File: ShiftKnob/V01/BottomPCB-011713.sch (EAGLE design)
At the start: 39 parts, among them IC2 7805DT, Q1 16MHz, Q2 MOSFET-NCHANNELSMD, Q3 MOSFET-NCHANNELSMD, Q4 MOSFET-NCHANNELSMD, Q5 MOSFET-NCHANNELSMD, Q6 MOSFET-NCHANNELSMD, U1 ATMEGA328

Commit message: preliminarily finalized. added silk screen labels. may still add mounting holes
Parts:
- JP2: device SparkFun:ARDUINO_SERIAL_PROGRAMPTH -> SparkFun-Connectors:M06SIP
- U$11: value LOGO-SFENEW -> LOGO-SFESK; device SparkFun:LOGO-SFENEW -> SparkFun:LOGO-SFESK
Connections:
- net DTR: now also JP2.1; no longer JP2.DTR
- net GND: now also JP2.5, JP2.6; no longer JP2.CTS, JP2.GND
- net RXI: now also JP2.3; no longer JP2.TXO
- net TXO: now also JP2.2; no longer JP2.RXI
- net VUSB: now also JP2.4; no longer JP2.VCC
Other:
- moved on the sheet: JP2
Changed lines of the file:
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@@
 <part name="C1" library="SparkFun" deviceset="CAP" device="0402-CAP" value="0.1uF"/>
 <part name="GND7" library="SparkFun" deviceset="GND" device=""/>
-<part name="U$11" library="SparkFun" deviceset="LOGO-SFE" device="NEW"/>
+<part name="U$11" library="SparkFun" deviceset="LOGO-SFE" device="SK" value="LOGO-SFESK"/>
 <part name="P+11" library="SparkFun" deviceset="3.3V" device="" value="VCC"/>
 <part name="P+15" library="SparkFun" deviceset="3.3V" device="" value="VCC"/>
@@
 <part name="P+1" library="SparkFun" deviceset="3.3V" device="" value="VCC"/>
 <part name="GND5" library="SparkFun" deviceset="GND" device=""/>
-<part name="JP2" library="SparkFun" deviceset="ARDUINO_SERIAL_PROGRAM" device="PTH" value="FTDI Basic"/>
+<part name="JP2" library="SparkFun-Connectors" deviceset="M06" device="SIP" value="FTDI Basic"/>
 <part name="C2" library="SparkFun" deviceset="CAP" device="0402-CAP" value="0.1uF"/>
 <part name="U$3" library="SparkFun" deviceset="OSHW-LOGO" device="S"/>
@@
 <wire x1="25.4" y1="195.58" x2="33.02" y2="195.58" width="0.1524" layer="91"/>
 <label x="27.94" y="195.58" size="1.778" layer="95"/>
-<pinref part="JP2" gate="G$1" pin="CTS"/>
+<pinref part="JP2" gate="G$1" pin="5"/>
 </segment>
 <segment>
 <wire x1="25.4" y1="198.12" x2="33.02" y2="198.12" width="0.1524" layer="91"/>
 <label x="27.94" y="198.12" size="1.778" layer="95"/>
-<pinref part="JP2" gate="G$1" pin="GND"/>
+<pinref part="JP2" gate="G$1" pin="6"/>
 </segment>
 <segment>
@@
 <wire x1="25.4" y1="187.96" x2="33.02" y2="187.96" width="0.1524" layer="91"/>
 <label x="27.94" y="187.96" size="1.778" layer="95"/>
-<pinref part="JP2" gate="G$1" pin="RXI"/>
+<pinref part="JP2" gate="G$1" pin="2"/>
 </segment>
 </net>
@@
 <wire x1="25.4" y1="185.42" x2="33.02" y2="185.42" width="0.1524" layer="91"/>
 <label x="27.94" y="185.42" size="1.778" layer="95"/>
-<pinref part="JP2" gate="G$1" pin="DTR"/>
+<pinref part="JP2" gate="G$1" pin="1"/>
 </segment>
 <segment>
@@
 <wire x1="25.4" y1="190.5" x2="33.02" y2="190.5" width="0.1524" layer="91"/>
 <label x="27.94" y="190.5" size="1.778" layer="95"/>
-<pinref part="JP2" gate="G$1" pin="TXO"/>
+<pinref part="JP2" gate="G$1" pin="3"/>
 </segment>
 <segment>
@@
 <wire x1="25.4" y1="193.04" x2="33.02" y2="193.04" width="0.1524" layer="91"/>
 <label x="27.94" y="193.04" size="1.778" layer="95"/>
-<pinref part="JP2" gate="G$1" pin="VCC"/>
-</segment>
-<segment>
+<pinref part="JP2" gate="G$1" pin="4"/>
+</segment>
+<segment>

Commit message: change diodes to match. add silk screen for polarity marking.
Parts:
- D1: value MBRA140 -> MBR0520LT; device SparkFun-DiscreteSemi:MBRA140 -> diode:MBR0520LT
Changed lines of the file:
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@@
 <part name="VCC2" library="SparkFun" deviceset="3.3V" device="" value="VCC"/>
 <part name="JP4" library="SparkFun-Connectors" deviceset="M02" device="-JST-2MM-SMT" value="PWM Motor Connection"/>
-<part name="D1" library="SparkFun-DiscreteSemi" deviceset="MBRA140" device=""/>
+<part name="D1" library="diode" deviceset="MBR0520LT" device=""/>
 <part name="GND8" library="SparkFun" deviceset="GND" device=""/>
 <part name="LED1" library="SparkFun" deviceset="LED-TRICOLOR" device=""/>

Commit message: attach button to arduino pin 2 rather than 12 to use internal interrupt. adjust board accordingly. remove resistor and use internal resistor of atemga328.
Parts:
- removed R12: 10k, SparkFun-Passives:RESISTOR0402-RES
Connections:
- net D12: no longer R12.1, S1.3, S1.4
- net D2: now also S1.3, S1.4
- net VCC: no longer R12.2
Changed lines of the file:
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@@
 <part name="GND13" library="SparkFun" deviceset="GND" device=""/>
 <part name="GND14" library="SparkFun" deviceset="GND" device=""/>
-<part name="P+2" library="SparkFun" deviceset="3.3V" device="" value="VCC"/>
-<part name="R12" library="SparkFun-Passives" deviceset="RESISTOR" device="0402-RES" value="10k"/>
 <part name="D2" library="diode" deviceset="MBR0520LT" device=""/>
 <part name="VUSB" library="SparkFun-Aesthetics" deviceset="VCC" device="" value="VUSB"/>
@@
 <instance part="GND13" gate="1" x="160.02" y="58.42"/>
 <instance part="GND14" gate="1" x="175.26" y="43.18"/>
-<instance part="P+2" gate="G$1" x="119.38" y="71.12" smashed="yes">
-<attribute name="VALUE" x="120.904" y="74.676" size="1.778" layer="96"/>
-</instance>
-<instance part="R12" gate="G$1" x="119.38" y="63.5" smashed="yes" rot="R90">
-<attribute name="NAME" x="125.73" y="67.0814" size="1.778" layer="95" rot="R180"/>
-<attribute name="VALUE" x="125.73" y="61.722" size="1.778" layer="96" rot="R180"/>
-</instance>
 <instance part="D2" gate="G$1" x="149.86" y="187.96" rot="MR0"/>
 <instance part="VUSB" gate="1" x="157.48" y="193.04" rot="MR0"/>
@@
 </segment>
 <segment>
-<pinref part="R12" gate="G$1" pin="2"/>
-<pinref part="P+2" gate="G$1" pin="3.3V"/>
-<wire x1="119.38" y1="71.12" x2="119.38" y2="68.58" width="0.1524" layer="91"/>
-</segment>
-<segment>
 <pinref part="D2" gate="G$1" pin="C"/>
 <wire x1="147.32" y1="187.96" x2="139.7" y2="187.96" width="0.1524" layer="91"/>
@@
 <label x="101.6" y="76.2" size="1.778" layer="95"/>
 <pinref part="U1" gate="G$1" pin="PB4(MISO)"/>
-<pinref part="S1" gate="S" pin="3"/>
-<wire x1="99.06" y1="76.2" x2="116.84" y2="76.2" width="0.1524" layer="91"/>
-<wire x1="116.84" y1="76.2" x2="116.84" y2="58.42" width="0.1524" layer="91"/>
-<wire x1="116.84" y1="58.42" x2="116.84" y2="53.34" width="0.1524" layer="91"/>
-<pinref part="S1" gate="S" pin="4"/>
-<wire x1="116.84" y1="58.42" x2="119.38" y2="58.42" width="0.1524" layer="91"/>
-<wire x1="119.38" y1="58.42" x2="119.38" y2="53.34" width="0.1524" layer="91"/>
-<junction x="116.84" y="58.42"/>
-<pinref part="R12" gate="G$1" pin="1"/>
-<junction x="119.38" y="58.42"/>
+<wire x1="99.06" y1="76.2" x2="111.76" y2="76.2" width="0.1524" layer="91"/>
 </segment>
 </net>
@@
 <net name="D2" class="0">
 <segment>
-<wire x1="99.06" y1="104.14" x2="109.22" y2="104.14" width="0.1524" layer="91"/>
+<wire x1="99.06" y1="104.14" x2="116.84" y2="104.14" width="0.1524" layer="91"/>
 <label x="101.6" y="104.14" size="1.778" layer="95"/>
 <pinref part="U1" gate="G$1" pin="PD2(INT0)"/>
-</segment>
-</net>
+<pinref part="S1" gate="S" pin="3"/>
+<pinref part="S1" gate="S" pin="4"/>
+<wire x1="119.38" y1="58.42" x2="119.38" y2="53.34" width="0.1524" layer="91"/>
+<wire x1="116.84" y1="58.42" x2="119.38" y2="58.42" width="0.1524" layer="91"/>
+<wire x1="116.84" y1="58.42" x2="116.84" y2="53.34" width="0.1524" layer="91"/>
+<wire x1="116.84" y1="58.42" x2="116.84" y2="104.14" width="0.1524" layer="91"/>
+</segment>
+</net>

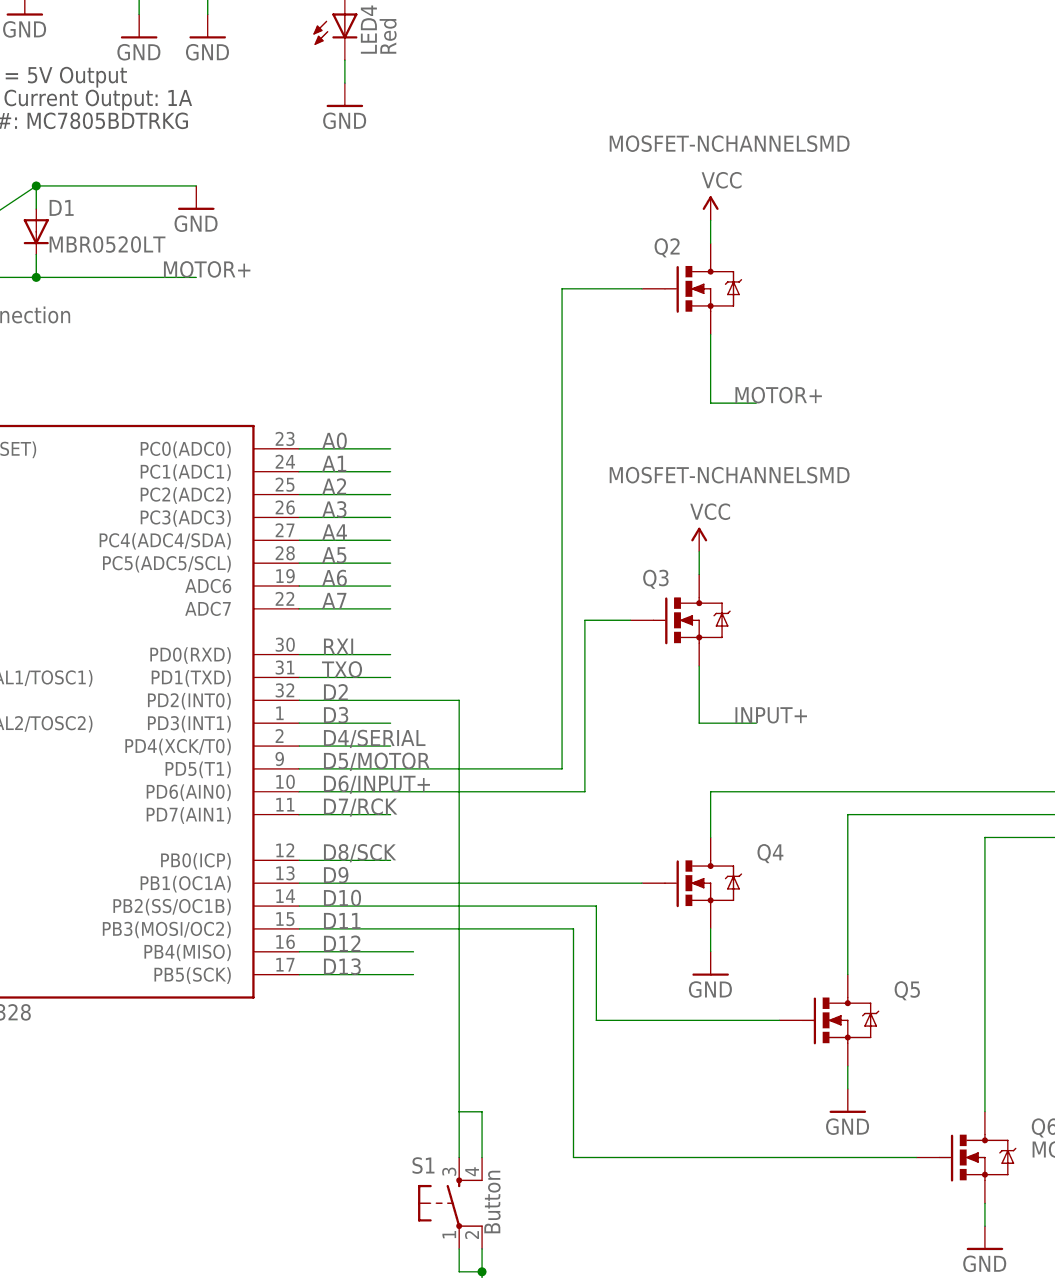
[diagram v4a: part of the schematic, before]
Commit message: fix board layout and schematic to properly setup MOSFETs. regenerate Gerber files. Change N-Channel MOSFET to P-Channel for 7segment brightness control (INPUT+)
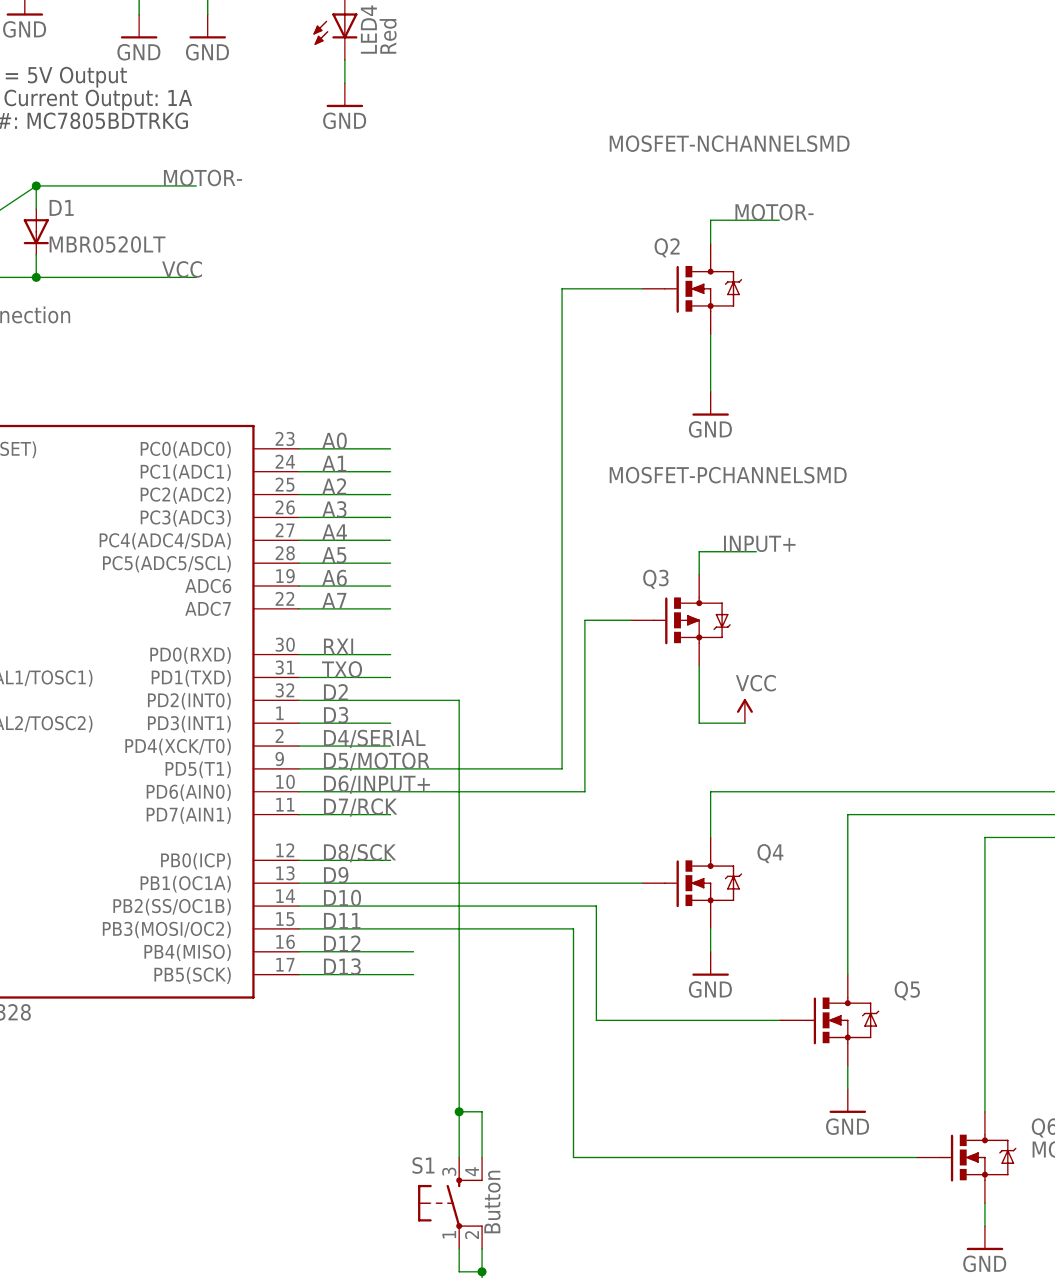
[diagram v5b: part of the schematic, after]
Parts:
- Q3: value MOSFET-NCHANNELSMD -> MOSFET-PCHANNELSMD; device SparkFun-DiscreteSemi:MOSFET-NCHANNELSMD -> SparkFun-DiscreteSemi:MOSFET-PCHANNELSMD
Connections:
- removed net MOTOR+: D1.C, JP4.1, Q2.S
- new net MOTOR-: D1.A, JP4.2, Q2.D
- net GND: now also Q2.S; no longer D1.A, JP4.2
- net INPUT+: now also Q3.D; no longer Q3.S
- net VCC: now also D1.C, JP4.1, Q3.S; no longer Q2.D, Q3.D
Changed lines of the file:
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@@
 <setting verticaltext="up"/>
 </settings>
-<grid distance="0.1" unitdist="inch" unit="inch" style="lines" multiple="1" display="no" altdistance="0.01" altunitdist="inch" altunit="inch"/>
+<grid distance="0.05" unitdist="inch" unit="inch" style="lines" multiple="1" display="no" altdistance="0.01" altunitdist="inch" altunit="inch"/>
 <layers>
 <layer number="1" name="Top" color="4" fill="1" visible="no" active="no"/>
@@
 <part name="R9" library="SparkFun-Resistors" deviceset="RESISTOR" device="0805-RES" value="100"/>
 <part name="Q2" library="SparkFun-DiscreteSemi" deviceset="MOSFET-NCHANNEL" device="SMD"/>
-<part name="Q3" library="SparkFun-DiscreteSemi" deviceset="MOSFET-NCHANNEL" device="SMD"/>
-<part name="VCC1" library="SparkFun" deviceset="3.3V" device="" value="VCC"/>
-<part name="VCC2" library="SparkFun" deviceset="3.3V" device="" value="VCC"/>
+<part name="Q3" library="SparkFun-DiscreteSemi" deviceset="MOSFET-PCHANNEL" device="SMD"/>
 <part name="JP4" library="SparkFun-Connectors" deviceset="M02" device="-JST-2MM-SMT" value="PWM Motor Connection"/>
 <part name="D1" library="diode" deviceset="MBR0520LT" device=""/>
-<part name="GND8" library="SparkFun" deviceset="GND" device=""/>
 <part name="LED1" library="SparkFun" deviceset="LED-TRICOLOR" device=""/>
 <part name="R6" library="SparkFun-Resistors" deviceset="RESISTOR" device="0805-RES" value="50"/>
@@
 <part name="VUSB" library="SparkFun-Aesthetics" deviceset="VCC" device="" value="VUSB"/>
 <part name="VCC4" library="SparkFun" deviceset="3.3V" device="" value="VCC"/>
+<part name="GND8" library="SparkFun" deviceset="GND" device=""/>
+<part name="VCC1" library="SparkFun" deviceset="3.3V" device="" value="VCC"/>
 </parts>
 <sheets>
@@
 <attribute name="VALUE" x="133.35" y="128.27" size="1.778" layer="96"/>
 </instance>
-<instance part="VCC1" gate="G$1" x="144.78" y="157.48"/>
-<instance part="VCC2" gate="G$1" x="143.51" y="120.65"/>
 <instance part="JP4" gate="G$1" x="50.8" y="151.13"/>
 <instance part="D1" gate="G$1" x="69.85" y="156.21" smashed="yes" rot="R270">
@@
 <attribute name="VALUE" x="71.12" y="153.8986" size="1.778" layer="96"/>
 </instance>
-<instance part="GND8" gate="1" x="87.63" y="158.75"/>
 <instance part="LED1" gate="G$1" x="248.92" y="129.54" rot="R90"/>
 <instance part="R6" gate="G$1" x="243.84" y="109.22" rot="R90"/>
@@
 <instance part="VUSB" gate="1" x="157.48" y="193.04" rot="MR0"/>
 <instance part="VCC4" gate="G$1" x="139.7" y="193.04" rot="MR0"/>
+<instance part="GND8" gate="1" x="144.78" y="135.89"/>
+<instance part="VCC1" gate="G$1" x="148.59" y="101.6"/>
 </instances>
 <busses>
@@
 </segment>
 <segment>
-<pinref part="Q3" gate="G$1" pin="S"/>
-<wire x1="143.51" y1="107.95" x2="143.51" y2="101.6" width="0.1524" layer="91"/>
-<wire x1="143.51" y1="101.6" x2="149.86" y2="101.6" width="0.1524" layer="91"/>
-<label x="147.32" y="101.6" size="1.778" layer="95"/>
+<pinref part="Q3" gate="G$1" pin="D"/>
+<wire x1="143.51" y1="118.11" x2="143.51" y2="120.65" width="0.1524" layer="91"/>
+<wire x1="143.51" y1="120.65" x2="149.86" y2="120.65" width="0.1524" layer="91"/>
+<label x="146.05" y="120.65" size="1.778" layer="95"/>
 </segment>
 </net>
@@
 </segment>
 <segment>
-<pinref part="JP4" gate="G$1" pin="2"/>
-<wire x1="58.42" y1="153.67" x2="69.85" y2="161.29" width="0.1524" layer="91"/>
-<pinref part="D1" gate="G$1" pin="A"/>
-<wire x1="69.85" y1="161.29" x2="87.63" y2="161.29" width="0.1524" layer="91"/>
-<wire x1="69.85" y1="158.75" x2="69.85" y2="161.29" width="0.1524" layer="91"/>
-<junction x="69.85" y="161.29"/>
-<pinref part="GND8" gate="1" pin="GND"/>
-</segment>
-<segment>
 <pinref part="Q4" gate="G$1" pin="S"/>
 <wire x1="144.78" y1="78.74" x2="144.78" y2="76.2" width="0.1524" layer="91"/>
@@
 <wire x1="175.26" y1="48.26" x2="175.26" y2="45.72" width="0.1524" layer="91"/>
 <pinref part="GND14" gate="1" pin="GND"/>
+</segment>
+<segment>
+<pinref part="Q2" gate="G$1" pin="S"/>
+<wire x1="144.78" y1="144.78" x2="144.78" y2="138.43" width="0.1524" layer="91"/>
+<pinref part="GND8" gate="1" pin="GND"/>
 </segment>
 </net>
@@
 </segment>
 <segment>
-<pinref part="Q3" gate="G$1" pin="D"/>
-<wire x1="143.51" y1="118.11" x2="143.51" y2="120.65" width="0.1524" layer="91"/>
-<pinref part="VCC2" gate="G$1" pin="3.3V"/>
-</segment>
-<segment>
-<pinref part="Q2" gate="G$1" pin="D"/>
-<wire x1="144.78" y1="154.94" x2="144.78" y2="157.48" width="0.1524" layer="91"/>
-<pinref part="VCC1" gate="G$1" pin="3.3V"/>
-</segment>
-<segment>
 <pinref part="LED2" gate="G$1" pin="A"/>
 <wire x1="195.58" y1="144.78" x2="195.58" y2="142.24" width="0.1524" layer="91"/>
@@
 <wire x1="139.7" y1="187.96" x2="139.7" y2="193.04" width="0.1524" layer="91"/>
 <pinref part="VCC4" gate="G$1" pin="3.3V"/>
+</segment>
+<segment>
+<pinref part="JP4" gate="G$1" pin="1"/>
+<wire x1="58.42" y1="151.13" x2="69.85" y2="151.13" width="0.1524" layer="91"/>
+<label x="83.82" y="151.13" size="1.778" layer="95"/>
+<pinref part="D1" gate="G$1" pin="C"/>
+<wire x1="69.85" y1="151.13" x2="87.63" y2="151.13" width="0.1524" layer="91"/>
+<wire x1="69.85" y1="153.67" x2="69.85" y2="151.13" width="0.1524" layer="91"/>
+<junction x="69.85" y="151.13"/>
+</segment>
+<segment>
+<pinref part="Q3" gate="G$1" pin="S"/>
+<wire x1="143.51" y1="107.95" x2="143.51" y2="101.6" width="0.1524" layer="91"/>
+<pinref part="VCC1" gate="G$1" pin="3.3V"/>
+<wire x1="148.59" y1="101.6" x2="143.51" y2="101.6" width="0.1524" layer="91"/>
 </segment>
 </net>
@@
 <wire x1="116.84" y1="58.42" x2="116.84" y2="53.34" width="0.1524" layer="91"/>
 <wire x1="116.84" y1="58.42" x2="116.84" y2="104.14" width="0.1524" layer="91"/>
+<junction x="116.84" y="58.42"/>
 </segment>
 </net>
@@
 </segment>
 </net>
-<net name="MOTOR+" class="0">
-<segment>
-<pinref part="Q2" gate="G$1" pin="S"/>
-<wire x1="144.78" y1="144.78" x2="144.78" y2="137.16" width="0.1524" layer="91"/>
-<wire x1="144.78" y1="137.16" x2="149.86" y2="137.16" width="0.1524" layer="91"/>
-<label x="147.32" y="137.16" size="1.778" layer="95"/>
-</segment>
-<segment>
-<pinref part="JP4" gate="G$1" pin="1"/>
-<wire x1="58.42" y1="151.13" x2="69.85" y2="151.13" width="0.1524" layer="91"/>
-<label x="83.82" y="151.13" size="1.778" layer="95"/>
-<pinref part="D1" gate="G$1" pin="C"/>
-<wire x1="69.85" y1="151.13" x2="87.63" y2="151.13" width="0.1524" layer="91"/>
-<wire x1="69.85" y1="153.67" x2="69.85" y2="151.13" width="0.1524" layer="91"/>
-<junction x="69.85" y="151.13"/>
-</segment>
-</net>
 <net name="N$7" class="0">
 <segment>
@@
 </segment>
 </net>
+<net name="MOTOR-" class="0">
+<segment>
+<pinref part="JP4" gate="G$1" pin="2"/>
+<wire x1="58.42" y1="153.67" x2="69.85" y2="161.29" width="0.1524" layer="91"/>
+<pinref part="D1" gate="G$1" pin="A"/>
+<wire x1="69.85" y1="161.29" x2="87.63" y2="161.29" width="0.1524" layer="91"/>
+<wire x1="69.85" y1="158.75" x2="69.85" y2="161.29" width="0.1524" layer="91"/>
+<junction x="69.85" y="161.29"/>
+<label x="83.82" y="161.29" size="1.778" layer="95"/>
+</segment>
+<segment>
+<pinref part="Q2" gate="G$1" pin="D"/>
+<wire x1="144.78" y1="154.94" x2="144.78" y2="157.48" width="0.1524" layer="91"/>
+<wire x1="144.78" y1="157.48" x2="152.4" y2="157.48" width="0.1524" layer="91"/>
+<label x="147.32" y="157.48" size="1.778" layer="95"/>
+</segment>
+</net>

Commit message: update schematics with new Ford frame.
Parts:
- removed U$11: LOGO-SFESK, SparkFun:LOGO-SFESK
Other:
- note added: "01"
- note added: "Zachary Nelson znelson1@ford.com"
- note removed: "1"
- note removed: "Author: Zachary Nelson znelson1@ford.com"
- moved on the sheet: Q2, Q3, S1
